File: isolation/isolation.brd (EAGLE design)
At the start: 91.4 x 83 mm, 79 parts, among them IC1 XTLV61048DBVR, IC2 SN74HC14DRG3, IC3 SN74HCS32PWR, IC4 SN74HCS08DYYR, IC5 FDN359BN, IC6 FDN359BN, IC7 FDN359BN, IC8 FDN359BN, J1 S4B-XH-A_LF__SN_, J2 S4B-XH-A_LF__SN_, J3 S4B-XH-A_LF__SN_, J4 S4B-XH-A_LF__SN_, J5 S4B-XH-A_LF__SN_

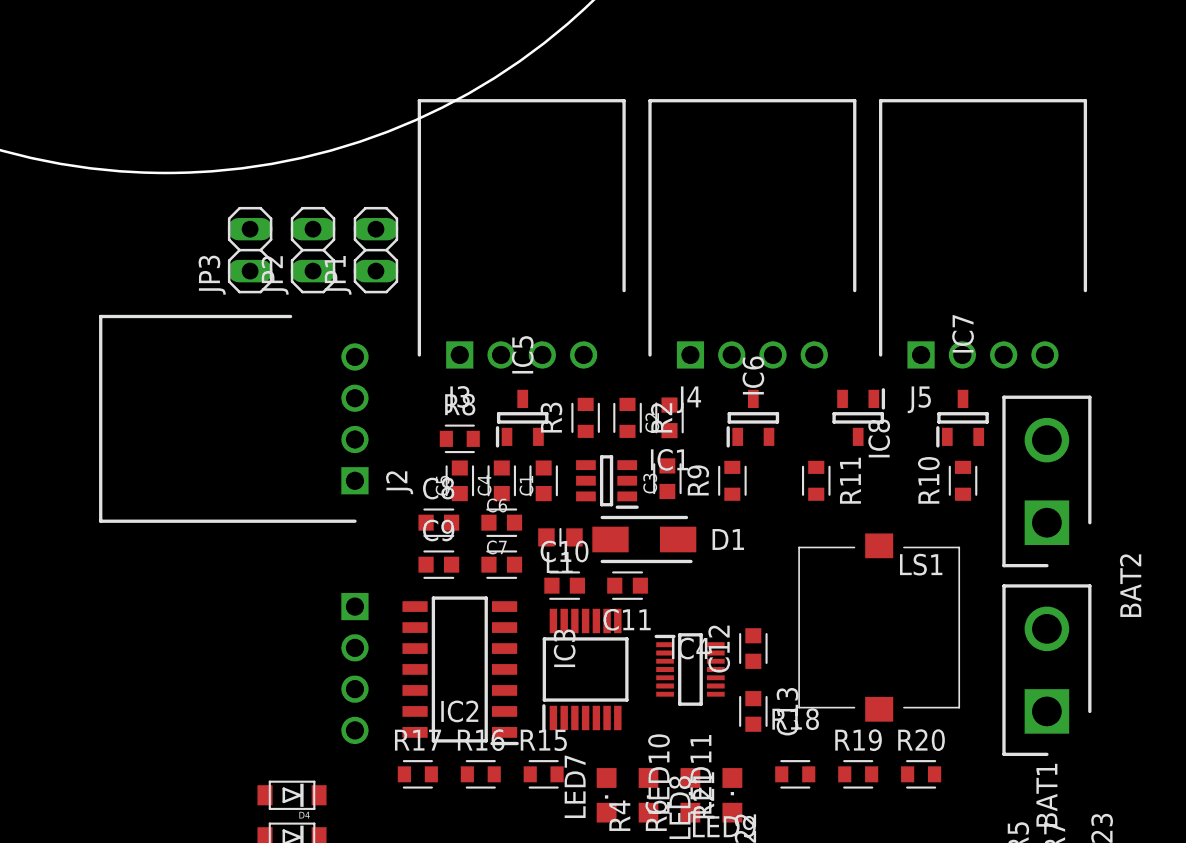
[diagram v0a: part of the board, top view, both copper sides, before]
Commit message: switch to JST-PH
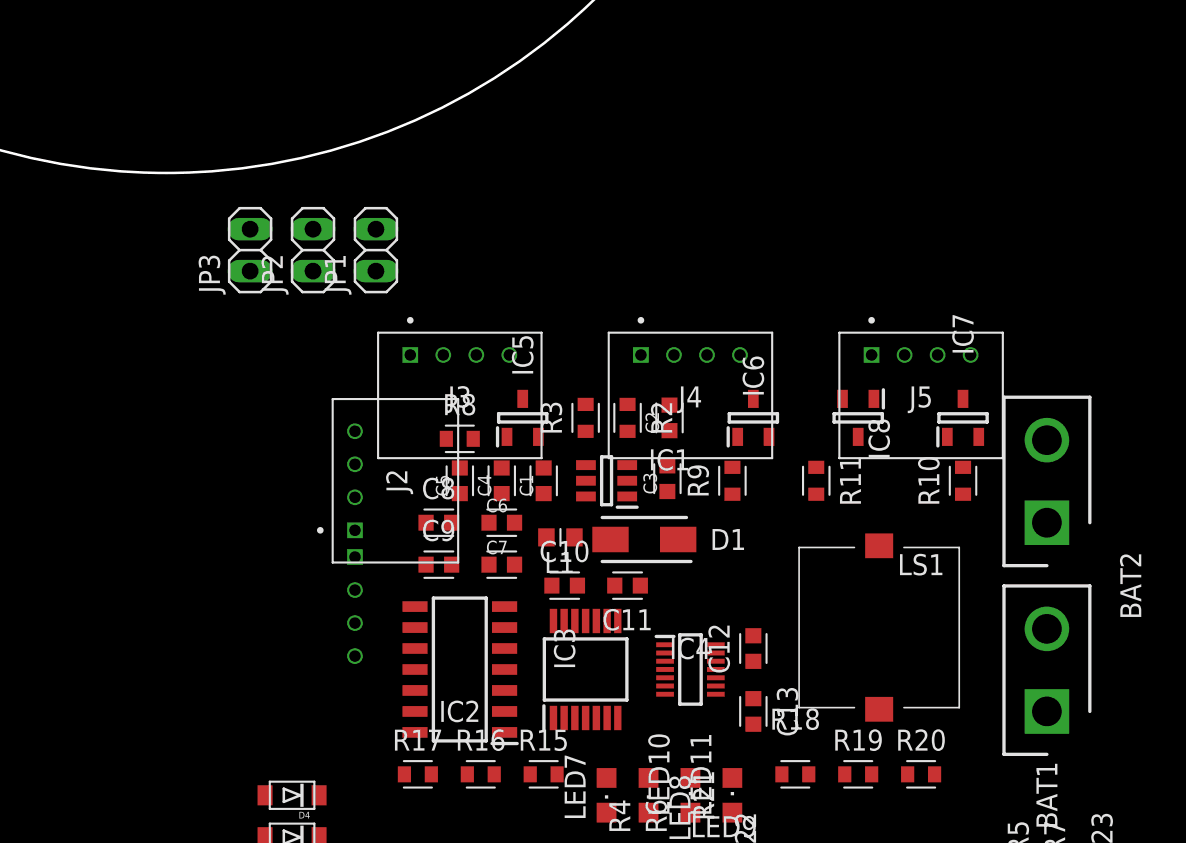
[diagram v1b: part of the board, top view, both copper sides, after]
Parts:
- J1, J2, J3, J4, J5: value S4B-XH-A_LF__SN_ -> S4B-PH-K-S(LF)(SN); device SamacSys_Parts:SHDRRA4W64P0X250_1X4_1240X1150 -> Headers:S4B-PH-K-S(LF)(SN)
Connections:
- net VDEP: no longer J4.1

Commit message: physically placed
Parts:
- BAT1, BAT2: value XT30UPB-M -> (none); device SamacSys_Parts:SHDR2W160P0X500_1X2_1020X520X1 -> adafruit:JST-PH-2-THM-RA
- moved LED3 139.2 mm to (-30.4, 12.3), turned to 270 degrees
- moved LED13 137.3 mm to (-28.4, 9.40)
- moved LED12 137.3 mm to (-30.5, 9.40), turned to 180 degrees
- moved LED2 136.5 mm to (-32.4, 9.40)
- moved R22 119.1 mm to (-27.9, 20.3)
- moved R21 116.3 mm to (-29.2, 17.8), turned to 0 degrees
- moved LED6 115.6 mm to (-16.5, 27.9), turned to 0 degrees
- moved R4 112.2 mm to (-30.5, 15.2)
- moved R6 112.2 mm to (-27.9, 15.2)
- moved LED14 111.7 mm to (23.9, 21.6), turned to 240 degrees
- moved LED4 111.6 mm to (24.8, 23.1), turned to 240 degrees
- moved R15 111.3 mm to (-15.0, 31.0), turned to 180 degrees
- moved LED8 111.0 mm to (-12.4, 27.9), turned to 0 degrees
- moved LED7 110.8 mm to (-14.5, 27.9), turned to 0 degrees
- moved R16 109.1 mm to (-11.7, 31.0), turned to 180 degrees
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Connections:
- net GND: now also BAT1.2, BAT2.2; no longer BAT1.1, BAT2.1
- net VBAT: now also BAT1.1, BAT2.1; no longer BAT1.2, BAT2.2
- net VDEP: now also J4.1
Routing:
- net VDEP: track 0.00 -> 84.6 mm
- net VBAT: track 0.00 -> 69.8 mm
- net EN1: track 0.00 -> 40.4 mm, vias 0 -> 1
- net FIRE1: track 0.00 -> 37.7 mm, vias 0 -> 1
- net FIRE2: track 0.00 -> 36.2 mm, vias 0 -> 1
- net PICKLE3: track 0.00 -> 29.5 mm, vias 0 -> 2
- net INVR1: track 0.00 -> 23.6 mm, vias 0 -> 2
- net BUZZ: track 0.00 -> 18.7 mm, vias 0 -> 2
- net INVR2: track 0.00 -> 17.1 mm, vias 0 -> 2
- net FIRE3: track 0.00 -> 17.1 mm, vias 0 -> 1
- net INVR3: track 0.00 -> 16.9 mm
- net N$11: track 0.00 -> 16.9 mm, vias 0 -> 2
- net EN2: track 0.00 -> 16.6 mm, vias 0 -> 1
- net N$2: track 0.00 -> 11.1 mm
- net N$12: track 0.00 -> 11.0 mm
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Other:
- board size 91.4 x 83 mm -> 74.5 x 74.5 mm

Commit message: manual routing complete
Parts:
- moved C12 9.31 mm to (11.0, 10.9), turned to 180 degrees
- moved C13 9.20 mm to (11.0, 13.3), turned to 180 degrees
- moved C9 3.70 mm to (1.52, 11.4), turned to 90 degrees
- moved C8 1.26 mm to (-1.02, 11.4), turned to 90 degrees
- moved IC4 0.25 mm to (6.60, 10.2)
- turned R12 to 180 degrees
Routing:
- net PICKLE1: track 4.54 -> 88.1 mm, vias 0 -> 4
- net PICKLE2: track 4.35 -> 83.7 mm, vias 0 -> 2
- net PICKLE3: track 29.5 -> 100.5 mm, vias 2 -> 4
- net RAVEN3: track 0.00 -> 70.3 mm, vias 0 -> 2
- net RAVEN2: track 0.00 -> 68.6 mm
- net RAVEN1: track 0.00 -> 62.1 mm
- net FIRE2: track 36.2 -> 85.4 mm, vias 1 -> 5
- net FIRE1: track 37.7 -> 86.4 mm, vias 1 -> 3
- net SAFE2: track 0.00 -> 47.7 mm, vias 0 -> 2
- net EN2: track 16.6 -> 57.7 mm, vias 1 -> 3
- net SAFE1: track 0.00 -> 34.9 mm, vias 0 -> 4
- net COM2: track 0.00 -> 34.7 mm, vias 0 -> 2
- net EN1: track 40.4 -> 73.4 mm, vias 1 -> 6
- net COM1: track 0.00 -> 26.6 mm, vias 0 -> 4
- net N$21: track 0.00 -> 26.0 mm
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
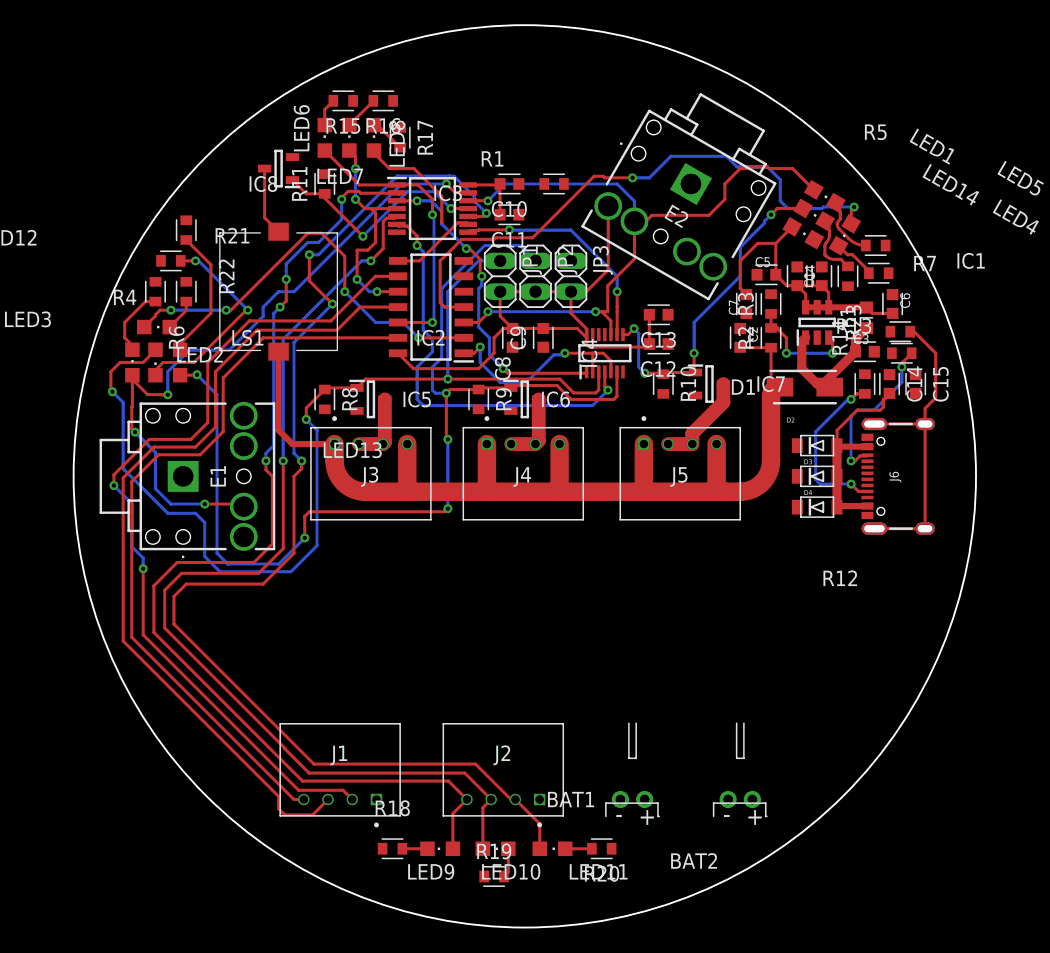
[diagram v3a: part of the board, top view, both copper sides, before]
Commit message: set board outline from dxf
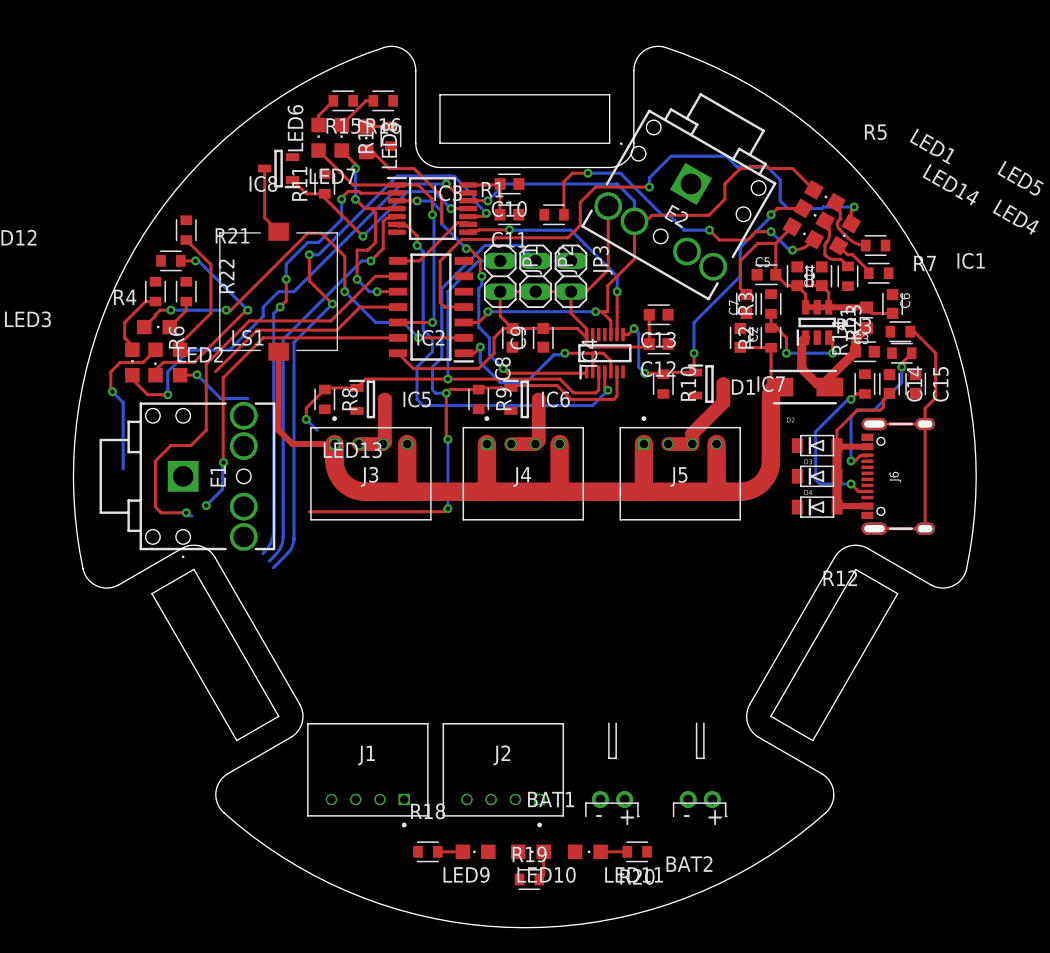
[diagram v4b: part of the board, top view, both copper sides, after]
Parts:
- moved BAT2 3.30 mm to (14.5, -26.7)
- moved R18 2.93 mm to (-8.00, -31.0)
- moved R20 2.93 mm to (9.27, -31.0)
- moved LED9 2.93 mm to (-4.06, -31.0)
- moved R19 2.93 mm to (0.38, -33.3)
- moved LED10 2.93 mm to (0.51, -31.0)
- moved LED11 2.93 mm to (5.21, -31.0)
- moved R1 2.54 mm to (2.41, 21.6)
- moved J1 2.29 mm to (-13.0, -26.7)
- moved BAT1 1.65 mm to (7.24, -26.7)
- moved R17 0.77 mm to (-11.0, 28.1), turned to 90 degrees
- moved LED8 0.65 mm to (-13.1, 27.8)
- moved LED7 0.63 mm to (-15.1, 27.9)
- moved LED6 0.51 mm to (-17.0, 27.9)
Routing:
- net PICKLE3: track 100.5 -> 49.1 mm, vias 4 -> 3
- net RAVEN2: track 68.6 -> 17.3 mm
- net PICKLE1: track 88.1 -> 37.5 mm, vias 4 -> 3
- net PICKLE2: track 83.7 -> 33.5 mm, vias 2 -> 1
- net RAVEN1: track 62.1 -> 26.9 mm, vias 0 -> 2
- net RAVEN3: track 70.3 -> 36.6 mm, vias 2 -> 1
- net FIRE1: track 86.4 -> 54.8 mm
- net N$1: track 0.00 -> 27.1 mm, vias 0 -> 4
- net FIRE2: track 85.4 -> 64.2 mm, vias 5 -> 4
- net EN1: track 73.4 -> 56.0 mm, vias 6 -> 4
- net SAFE2: track 47.7 -> 49.2 mm
- net INVR3: track 16.9 -> 18.1 mm
- net N$23: track 2.93 -> 2.03 mm
- net N$18: track 2.82 -> 3.44 mm
- net INVR1: track 23.7 -> 24.2 mm
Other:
- board size 74.5 x 74.5 mm -> 74.5 x 72.7 mm

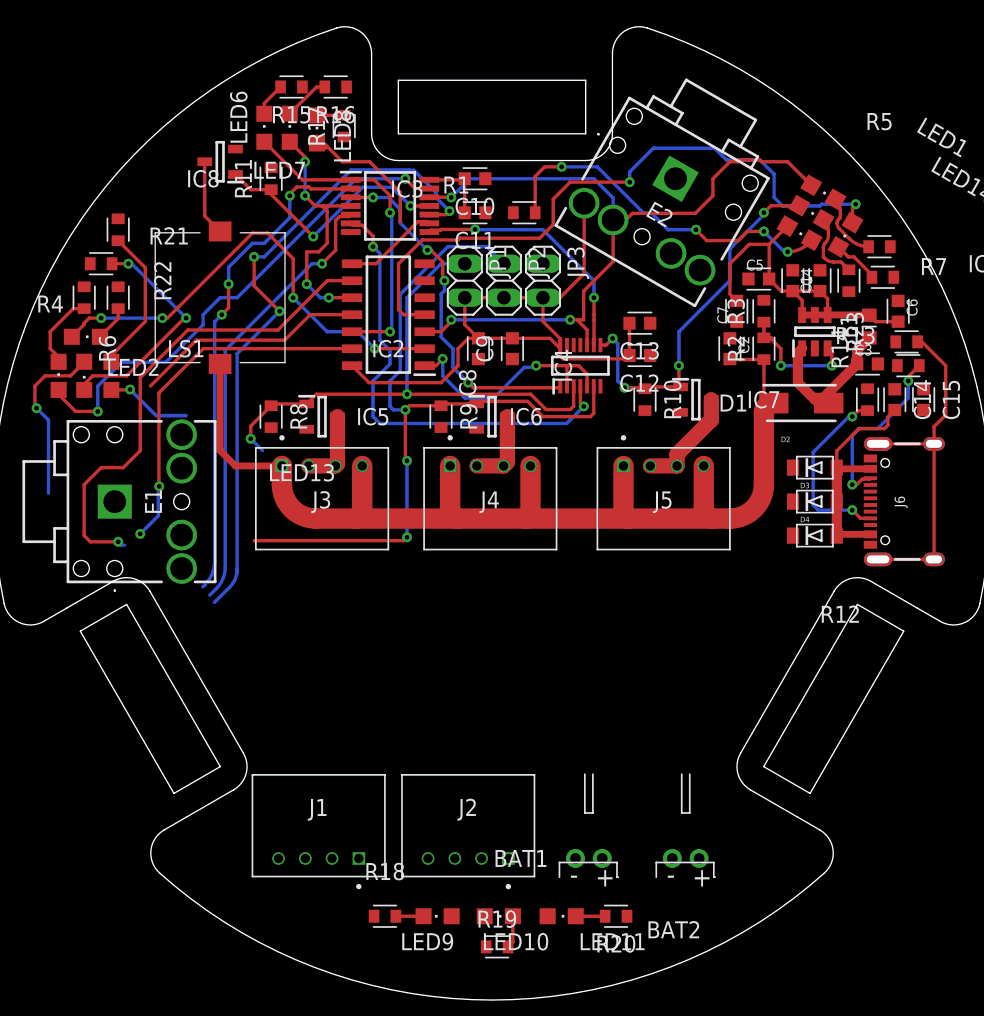
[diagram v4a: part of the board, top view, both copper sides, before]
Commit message: pads for ext power in
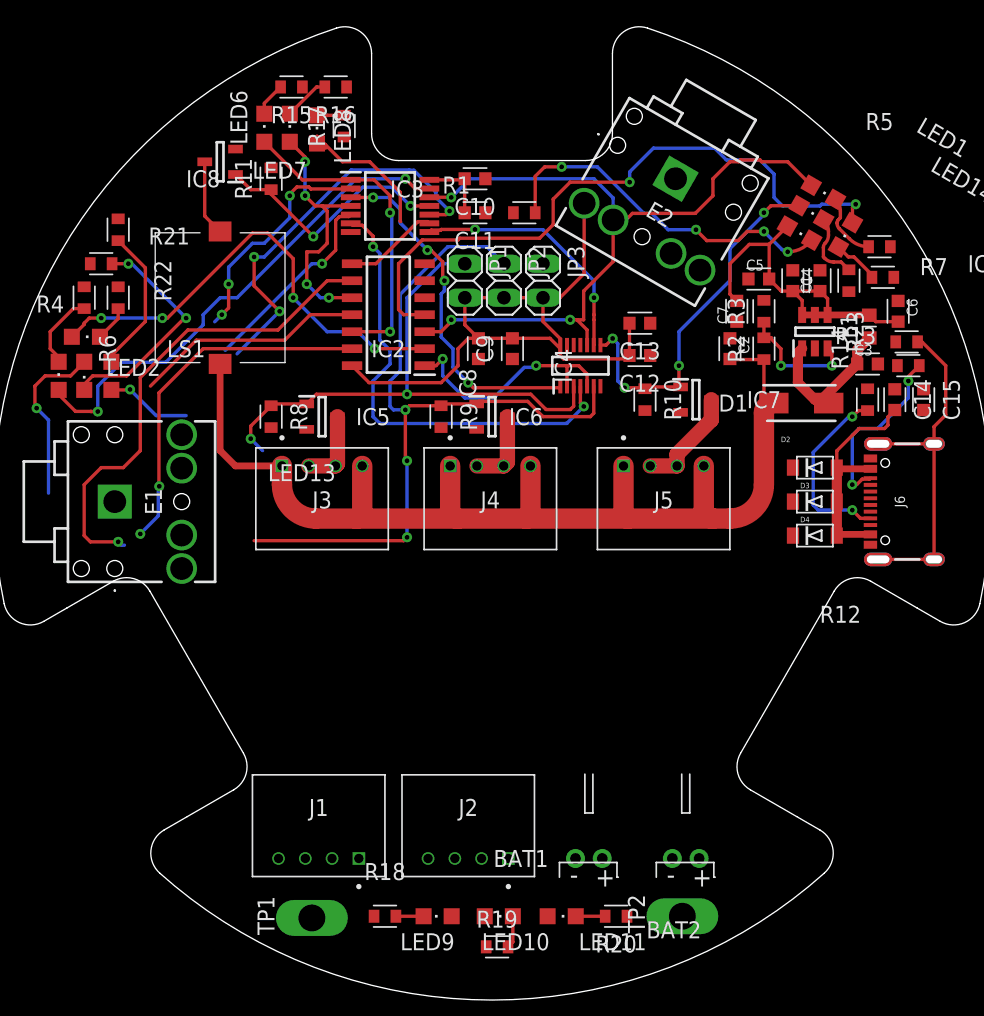
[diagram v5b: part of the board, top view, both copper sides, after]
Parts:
- added TP1, TP2: TPPAD1-20Y, testpad:P1-20Y
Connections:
- net GND: now also TP1.TP
- net VBAT: now also TP2.TP
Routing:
- net PICKLE1: track 37.5 -> 17.5 mm
- net PICKLE3: track 49.1 -> 29.8 mm
- net PICKLE2: track 33.5 -> 14.9 mm
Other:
- outline, holes or cut-outs redrawn
